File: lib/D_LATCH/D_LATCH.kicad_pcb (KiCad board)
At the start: 2 copper layers, 10 parts

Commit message: Rename EN/nEN into CLK/nCLK for D_LATCH
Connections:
- net EN renamed CLK
- net nEN renamed nCLK
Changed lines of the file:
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@@
 	(net 3 "D")
 	(net 4 "NOT1.intN")
-	(net 5 "EN")
+	(net 5 "CLK")
 	(net 6 "nQ")
 	(net 7 "NOT1.intP")
-	(net 8 "nEN")
+	(net 8 "nCLK")
 	(net 9 "Q")
 	(net 10 "NOT3.intN")
@@
 			(layers "F.Cu" "F.Mask" "F.Paste")
 			(roundrect_rratio 0.25)
-			(net 8 "nEN")
+			(net 8 "nCLK")
 			(pinfunction "G")
 			(pintype "inout")
@@
 			(layers "F.Cu" "F.Mask" "F.Paste")
 			(roundrect_rratio 0.25)
-			(net 5 "EN")
+			(net 5 "CLK")
 			(pinfunction "G")
 			(pintype "inout")
@@
 			(layers "F.Cu" "F.Mask" "F.Paste")
 			(roundrect_rratio 0.25)
-			(net 8 "nEN")
+			(net 8 "nCLK")
 			(pinfunction "G")
 			(pintype "inout")
@@
 			(layers "F.Cu" "F.Mask" "F.Paste")
 			(roundrect_rratio 0.25)
-			(net 5 "EN")
+			(net 5 "CLK")
 			(pinfunction "G")
 			(pintype "inout")

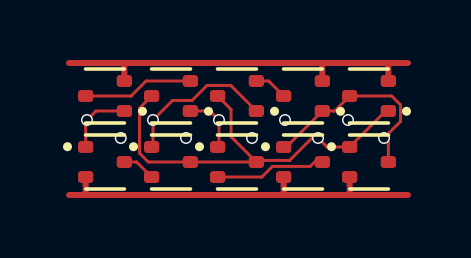
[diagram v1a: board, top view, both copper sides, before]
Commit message: All cells now use 1mm*4mm grid rather than 1.1mm*4.4mm
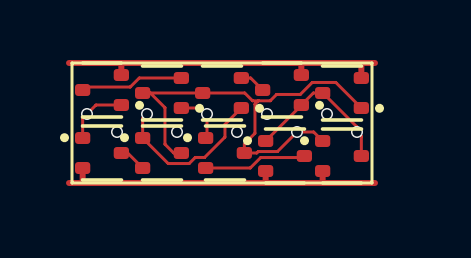
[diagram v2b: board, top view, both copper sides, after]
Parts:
- moved NOT2.N1 0.92 mm to (9.00, 3.10)
- moved NOT2.P1 0.91 mm to (9.00, 1.00)
- moved NOT3.P1 0.73 mm to (7.00, 0.90)
- moved NOT3.N1 0.63 mm to (7.10, 3.10)
- moved NOT3.P2 0.51 mm to (5.00, 1.00)
- moved NOT3.N2 0.50 mm to (5.10, 3.00)
- moved NOT1.N2 0.42 mm to (3.00, 3.00)
- moved NOT1.N1 0.32 mm to (1.00, 3.00)
- moved NOT1.P2 0.32 mm to (3.00, 1.00)
- moved NOT1.P1 0.22 mm to (1.00, 0.90)
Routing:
- net Q: track 6.92 -> 5.21 mm
- net GND: track 13.1 -> 11.6 mm
- net VDD: track 13.1 -> 11.6 mm
- net nQ: track 14.4 -> 15.8 mm

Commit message: Make the pads of my SOT523 footprint very slightly smaller, which is enough to route all the cells and leave the mosfets exactly on the grid
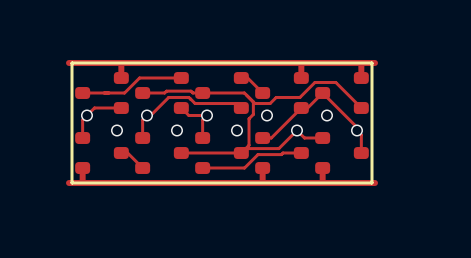
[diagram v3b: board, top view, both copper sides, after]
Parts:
- NOT1.N1, NOT1.N2, NOT1.P1, NOT1.P2, NOT2.N1, NOT2.P1, NOT3.N1, NOT3.N2, NOT3.P1, NOT3.P2: footprint Package_TO_SOT_SMD:SOT-523 -> RV523:SOT523
- moved NOT3.N1 0.14 mm to (7.00, 3.00)
- moved NOT2.N1 0.10 mm to (9.00, 3.00)
- moved NOT1.P1 0.10 mm to (1.00, 1.00)
- moved NOT3.P1 0.10 mm to (7.00, 1.00)
- moved NOT3.N2 0.10 mm to (5.00, 3.00)
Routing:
- net CLK: track 5.52 -> 4.35 mm

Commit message: Propagate MOSFET values to the cells' PCBs
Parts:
- NOT1.N1, NOT1.N2, NOT2.N1, NOT3.N1, NOT3.N2: value (none) -> NMOS
- NOT1.P1, NOT1.P2, NOT2.P1, NOT3.P1, NOT3.P2: value (none) -> PMOS
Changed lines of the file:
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@@
 			)
 		)
-		(property "Value" ""
+		(property "Value" "NMOS"
 			(at 0 0 0)
 			(layer "F.Fab")
@@
 			)
 		)
-		(property "Value" ""
+		(property "Value" "PMOS"
 			(at 0 0 180)
 			(layer "F.Fab")
@@
 			)
 		)
-		(property "Value" ""
+		(property "Value" "NMOS"
 			(at 0 0 0)
 			(layer "F.Fab")
@@
 			)
 		)
-		(property "Value" ""
+		(property "Value" "PMOS"
 			(at 0 0 180)
 			(layer "F.Fab")
@@
 			)
 		)
-		(property "Value" ""
+		(property "Value" "NMOS"
 			(at 0 0 0)
 			(layer "F.Fab")
@@
 			)
 		)
-		(property "Value" ""
+		(property "Value" "NMOS"
 			(at 0 0 0)
 			(layer "F.Fab")
@@
 			)
 		)
-		(property "Value" ""
+		(property "Value" "NMOS"
 			(at 0 0 0)
 			(layer "F.Fab")
@@
 			)
 		)
-		(property "Value" ""
+		(property "Value" "PMOS"
 			(at 0 0 180)
 			(layer "F.Fab")
@@
 			)
 		)
-		(property "Value" ""
+		(property "Value" "PMOS"
 			(at 0 0 180)
 			(layer "F.Fab")
@@
 			)
 		)
-		(property "Value" ""
-			(at 0 0 180)
-			(layer "F.Fab")
+		(property "Value" "PMOS"
+			(at 0 0 180)
+			(layer "F.Fab")
